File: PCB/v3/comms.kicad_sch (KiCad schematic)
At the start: 29 parts, among them J1 6437288-1, U4 TJA1051T/3, U5 TJA1027T/20

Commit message: pcb v3: lcsc numbers, lmr36520 buck
ap63200 vin abs max was under the smcj24ca clamp, j2 stud hand-fit
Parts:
- J1: LCSC (none) -> C574787
- R75, R79, R83: LCSC (none) -> C4216
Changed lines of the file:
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@@
+      )
+    )
+    (property "LCSC" "C4216"
+      (at 149.86 93.98 0)
+      (hide yes)
+      (effects
+        (font
+          (size 1.27 1.27)
+        )
       )
     )
@@
       )
     )
+    (property "LCSC" "C4216"
+      (at 233.68 93.98 0)
+      (hide yes)
+      (effects
+        (font
+          (size 1.27 1.27)
+        )
+      )
+    )
     (property "MPN" "0603WAF3302T5E"
       (at 233.68 93.98 0)
@@
       )
     )
+    (property "LCSC" "C4216"
+      (at 63.5 152.4 0)
+      (hide yes)
+      (effects
+        (font
+          (size 1.27 1.27)
+        )
+      )
+    )
     (property "MPN" "0603WAF3302T5E"
       (at 63.5 152.4 0)
@@
       (at 121.92 154.94 0)
       (hide yes)
+      (effects
+        (font
+          (size 1.27 1.27)
+        )
+      )
+    )
+    (property "LCSC" "C574787"
+      (at 121.92 154.94 0)
+      (hide yes)

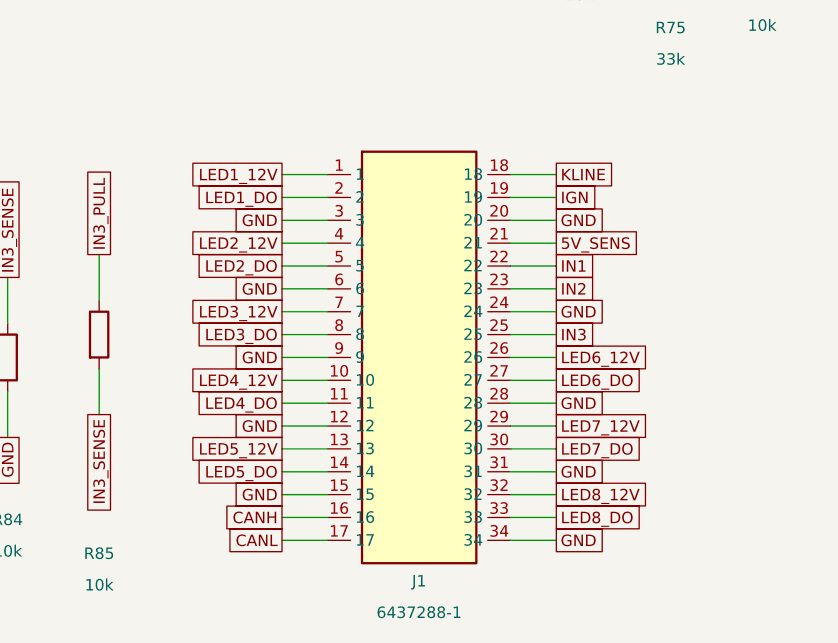
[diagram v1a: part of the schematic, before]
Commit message: pcb v3: j1 power row, gnd row
all LEDn_12V in row 1 over their switch, strip gnds in row 4, signals rows 2-3

Claude-Session: https://claude.ai/code/session_01MELKvCtSrN4XHin3AfxGm6
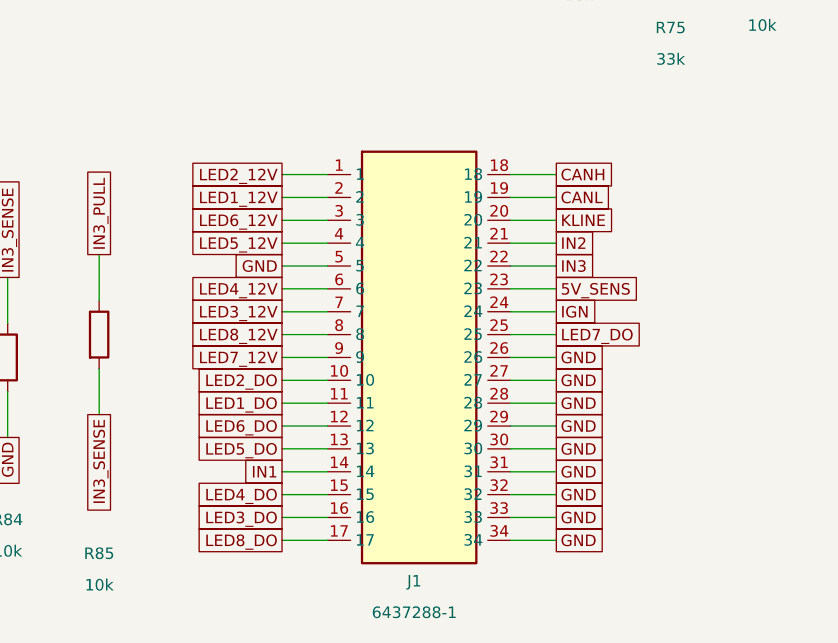
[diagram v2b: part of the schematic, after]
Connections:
- net 5V_SENS: now also J1.23; no longer J1.21
- net CANH: now also J1.18; no longer J1.16
- net CANL: now also J1.19; no longer J1.17
- net GND: now also J1.26, J1.27, J1.29, J1.30, J1.32, J1.33, J1.5; no longer J1.12, J1.15, J1.20, J1.24, J1.3, J1.6, J1.9
- net IGN: now also J1.24; no longer J1.19
- net IN1: now also J1.14; no longer J1.22
- net IN2: now also J1.21; no longer J1.23
- net IN3: now also J1.22; no longer J1.25
- net KLINE: now also J1.20; no longer J1.18
- net LED1_12V: now also J1.2; no longer J1.1
- net LED1_DO: now also J1.11; no longer J1.2
- net LED2_12V: now also J1.1; no longer J1.4
- net LED2_DO: now also J1.10; no longer J1.5
- net LED3_DO: now also J1.16; no longer J1.8
- net LED4_12V: now also J1.6; no longer J1.10
- net LED4_DO: now also J1.15; no longer J1.11
- net LED5_12V: now also J1.4; no longer J1.13
- net LED5_DO: now also J1.13; no longer J1.14
- net LED6_12V: now also J1.3; no longer J1.26
- net LED6_DO: now also J1.12; no longer J1.27
- net LED7_12V: now also J1.9; no longer J1.29
- net LED7_DO: now also J1.25; no longer J1.30
- net LED8_12V: now also J1.8; no longer J1.32
- net LED8_DO: now also J1.17; no longer J1.33
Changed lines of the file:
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@@
     (dnp no)
     (property "Reference" "J1"
-      (at 121.92 179.8 0)
+      (at 121.395 179.8 0)
       (effects
         (font
@@
     )
     (property "Value" "6437288-1"
-      (at 121.92 183.3 0)
+      (at 121.395 183.3 0)
       (effects
         (font
@@
     )
   )
-  (global_label "LED1_12V"
+  (global_label "LED2_12V"
     (shape passive)
     (at 106.68 134.62 180)
@@
     )
   )
-  (global_label "KLINE"
+  (global_label "CANH"
     (shape passive)
     (at 137.16 134.62 0)
@@
     )
   )
-  (global_label "LED1_DO"
+  (global_label "LED1_12V"
     (shape passive)
     (at 106.68 137.16 180)
@@
     )
   )
-  (global_label "IGN"
+  (global_label "CANL"
     (shape passive)
     (at 137.16 137.16 0)
@@
     )
   )
-  (global_label "GND"
+  (global_label "LED6_12V"
     (shape passive)
     (at 106.68 139.7 180)
@@
     )
   )
-  (global_label "GND"
+  (global_label "KLINE"
     (shape passive)
     (at 137.16 139.7 0)
@@
     )
   )
-  (global_label "LED2_12V"
+  (global_label "LED5_12V"
     (shape passive)
     (at 106.68 142.24 180)
@@
     )
   )
-  (global_label "5V_SENS"
+  (global_label "IN2"
     (shape passive)
     (at 137.16 142.24 0)
@@
     )
   )
-  (global_label "LED2_DO"
+  (global_label "GND"
     (shape passive)
     (at 106.68 144.78 180)
@@
     )
   )
-  (global_label "IN1"
+  (global_label "IN3"
     (shape passive)
     (at 137.16 144.78 0)
@@
     )
   )
-  (global_label "GND"
+  (global_label "LED4_12V"
     (shape passive)
     (at 106.68 147.32 180)
@@
     )
   )
-  (global_label "IN2"
+  (global_label "5V_SENS"
     (shape passive)
     (at 137.16 147.32 0)
@@
     )
   )
-  (global_label "GND"
+  (global_label "IGN"
     (shape passive)
     (at 137.16 149.86 0)
@@
     )
   )
-  (global_label "LED3_DO"
+  (global_label "LED8_12V"
     (shape passive)
     (at 106.68 152.4 180)
@@
     )
   )
-  (global_label "IN3"
+  (global_label "LED7_DO"
     (shape passive)
     (at 137.16 152.4 0)
@@
     )
   )
-  (global_label "GND"
+  (global_label "LED7_12V"
     (shape passive)
     (at 106.68 154.94 180)
@@
     )
   )
-  (global_label "LED6_12V"
+  (global_label "GND"
     (shape passive)
     (at 137.16 154.94 0)
@@
     )
   )
-  (global_label "LED4_12V"
+  (global_label "LED2_DO"
     (shape passive)
     (at 106.68 157.48 180)
@@
     )
   )
-  (global_label "LED6_DO"
+  (global_label "GND"
     (shape passive)
     (at 137.16 157.48 0)
@@
     )
   )
-  (global_label "LED4_DO"
+  (global_label "LED1_DO"
     (shape passive)
     (at 106.68 160.02 180)
@@
     )
   )
-  (global_label "GND"
+  (global_label "LED6_DO"
     (shape passive)
     (at 106.68 162.56 180)
@@
     )
   )
-  (global_label "LED7_12V"
+  (global_label "GND"
     (shape passive)
     (at 137.16 162.56 0)
@@
     )
   )
-  (global_label "LED5_12V"
+  (global_label "LED5_DO"
     (shape passive)
     (at 106.68 165.1 180)
@@
     )
   )
-  (global_label "LED7_DO"
+  (global_label "GND"
     (shape passive)
     (at 137.16 165.1 0)
@@
     )
   )
-  (global_label "LED5_DO"
+  (global_label "IN1"
     (shape passive)
     (at 106.68 167.64 180)
@@
     )
   )
-  (global_label "GND"
+  (global_label "LED4_DO"
     (shape passive)
     (at 106.68 170.18 180)
@@
     )
   )
-  (global_label "LED8_12V"
+  (global_label "GND"
     (shape passive)
     (at 137.16 170.18 0)
@@
     )
   )
-  (global_label "CANH"
+  (global_label "LED3_DO"
     (shape passive)
     (at 106.68 172.72 180)
@@
     )
   )
-  (global_label "LED8_DO"
+  (global_label "GND"
     (shape passive)
     (at 137.16 172.72 0)
@@
     )
   )
-  (global_label "CANL"
+  (global_label "LED8_DO"
     (shape passive)
     (at 106.68 175.26 180)
